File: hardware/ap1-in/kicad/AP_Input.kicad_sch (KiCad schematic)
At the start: 63 parts, among them J1 QWIIC ENTRADA, J2 QWIIC SALIDA, J3 I2C, J4 I1-I3, J5 I4-I6, J6 I7-I8, J7 COM, U1 TCA9554PWR

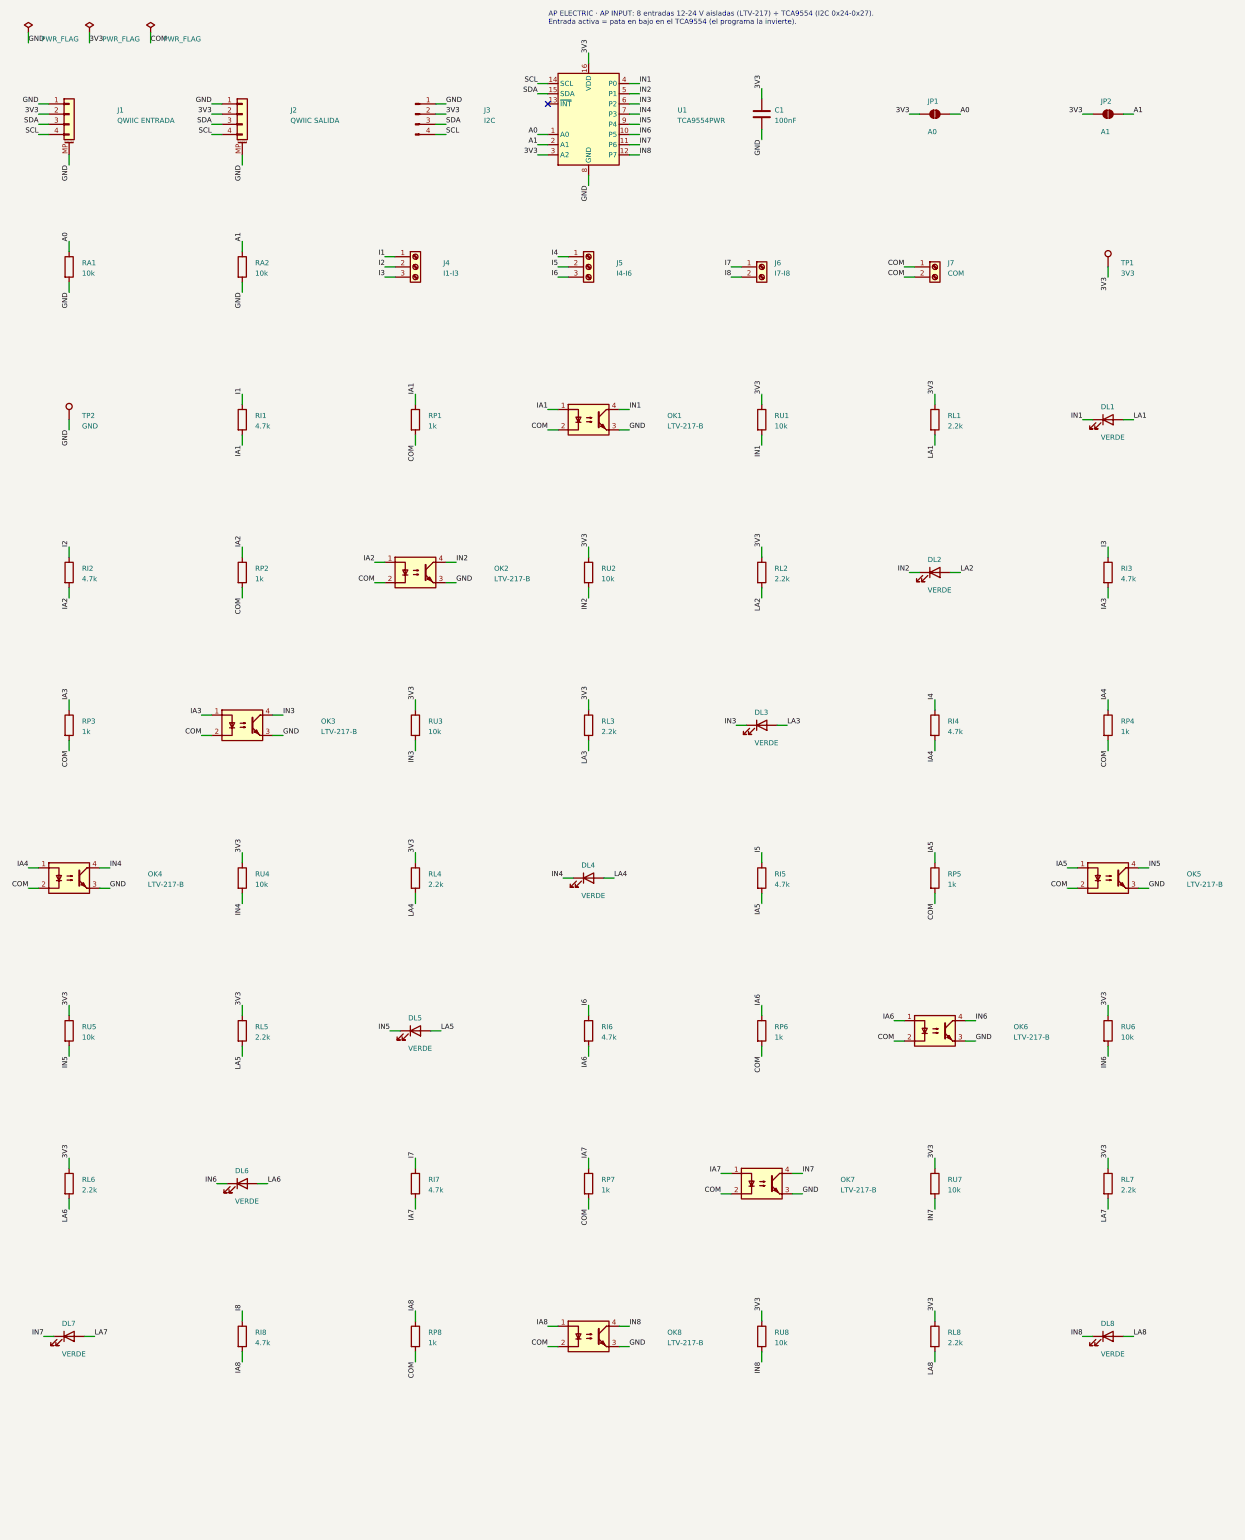
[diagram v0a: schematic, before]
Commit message: AP CONNECT: sin borneras en todas las placas, placa nueva AP PRO AI4 y guía de fabricantes
- Borneras de tornillo reemplazadas por conectores con cable y código LCSC verificado:
  XT60 (C98732), JST VH 2/3/4 (C160315/6/7), JST XH 2/3/4 (C158012, C144394/5), Qwiic
  en BASE, IND, PIX, DMX, PLANTILLA, AP INPUT, AP OUTPUT y DIST 4; zonas de potencia rehechas
- XT60 de la DIST 4 con la polaridad marcada en la huella (pata 1 = -, pata 2 = +)
- TCA9554PWR ya con código (C477924)
- ap1-ai4: 4 entradas 0-10 V / 4-20 mA con ADS1115 (C37593), +24 V para sensores de lazo
- Programa 1.7: lectura AI4, umbrales con acciones, Home Assistant, tarjeta en la app
- FABRICANTES.md: JLCPCB, PCBWay, Seeed, NextPCB, México; impresión 3D y tornillería
- Pedido JLCPCB con 10 placas (AP-0.2 retirada); ERC/DRC/DFM 0 en todas

Co-Authored-By: Claude Opus 5.5 <noreply@anthropic.com>
Claude-Session: https://claude.ai/code/session_01WVk3oGwfQfGTmAT2PMp8oW
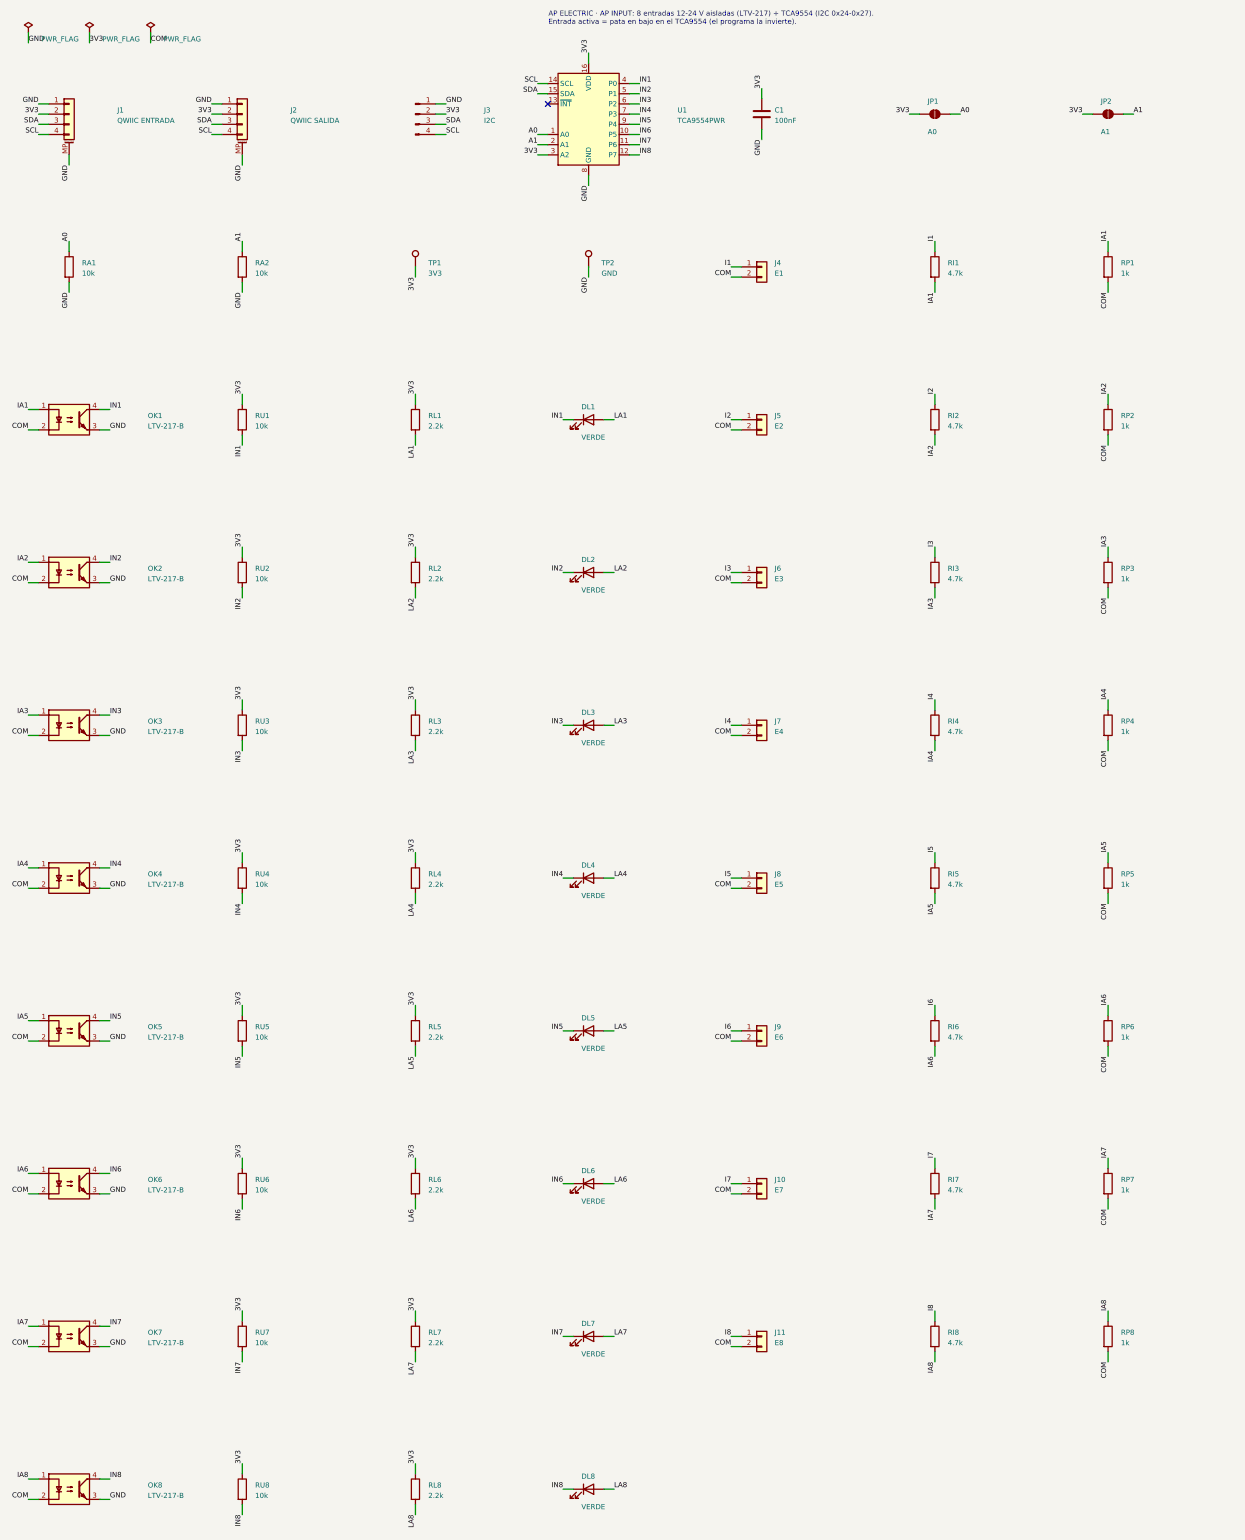
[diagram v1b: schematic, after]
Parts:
- added J10: E7, Connector_JST:JST_XH_B2B-XH-A_1x02_P2.50mm_Vertical, symbol Connector_Generic:Conn_01x02
- added J11: E8, Connector_JST:JST_XH_B2B-XH-A_1x02_P2.50mm_Vertical, symbol Connector_Generic:Conn_01x02
- added J8: E5, Connector_JST:JST_XH_B2B-XH-A_1x02_P2.50mm_Vertical, symbol Connector_Generic:Conn_01x02
- added J9: E6, Connector_JST:JST_XH_B2B-XH-A_1x02_P2.50mm_Vertical, symbol Connector_Generic:Conn_01x02
- J4: value I1-I3 -> E1; footprint TerminalBlock_Phoenix:TerminalBlock_Phoenix_MKDS-3-3-5.08_1x03_P5.08mm_Horizontal -> Connector_JST:JST_XH_B2B-XH-A_1x02_P2.50mm_Vertical; symbol Connector:Screw_Terminal_01x03 -> Connector_Generic:Conn_01x02; Funcion Entradas 1-3 -> Entrada 1: 1 = señal (+12-24 V), 2 = común (0 V de los sens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
- J5: value I4-I6 -> E2; footprint TerminalBlock_Phoenix:TerminalBlock_Phoenix_MKDS-3-3-5.08_1x03_P5.08mm_Horizontal -> Connector_JST:JST_XH_B2B-XH-A_1x02_P2.50mm_Vertical; symbol Connector:Screw_Terminal_01x03 -> Connector_Generic:Conn_01x02; Funcion Entradas 4-6 -> Entrada 2: 1 = señal (+12-24 V), 2 = común (0 V de los sens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
- J6: value I7-I8 -> E3; footprint TerminalBlock_Phoenix:TerminalBlock_Phoenix_MKDS-3-2-5.08_1x02_P5.08mm_Horizontal -> Connector_JST:JST_XH_B2B-XH-A_1x02_P2.50mm_Vertical; symbol Connector:Screw_Terminal_01x02 -> Connector_Generic:Conn_01x02; Funcion Entradas 7-8 -> Entrada 3: 1 = señal (+12-24 V), 2 = común (0 V de los sens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
- J7: value COM -> E4; footprint TerminalBlock_Phoenix:TerminalBlock_Phoenix_MKDS-3-2-5.08_1x02_P5.08mm_Horizontal -> Connector_JST:JST_XH_B2B-XH-A_1x02_P2.50mm_Vertical; symbol Connector:Screw_Terminal_01x02 -> Connector_Generic:Conn_01x02; Funcion Común de las entradas: el 0 V de la fuente de los sensores -> Entrada 4: 1 = señal (+12-24 V), 2 = común (0 V de los sens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
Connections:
- net COM: now also J4.2 (Pin_2), J5.2 (Pin_2), J6.2 (Pin_2), J10.2 (Pin_2), J11.2 (Pin_2), J8.2 (Pin_2), J9.2 (Pin_2); no longer J7.1 (Pin_1)
- net I2: now also J5.1 (Pin_1); no longer J4.2 (Pin_2)
- net I3: now also J6.1 (Pin_1); no longer J4.3 (Pin_3)
- net I4: now also J7.1 (Pin_1); no longer J5.1 (Pin_1)
- net I5: now also J8.1 (Pin_1); no longer J5.2 (Pin_2)
- net I6: now also J9.1 (Pin_1); no longer J5.3 (Pin_3)
- net I7: now also J10.1 (Pin_1); no longer J6.1 (Pin_1)
- net I8: now also J11.1 (Pin_1); no longer J6.2 (Pin_2)
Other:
- moved on the sheet: DL1, DL2, DL3, DL5, DL6, DL7, DL8, OK1, OK2, OK3, OK5, OK6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
